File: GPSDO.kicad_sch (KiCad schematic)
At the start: 87 parts, among them J1 Conn_Coaxial, J10 PROG, J2 GPS_CONN, J3 Conn_Coaxial, J4 Conn_Coaxial, J5 Conn_Coaxial, J6 Conn_Coaxial, J7 LCD_CONN, J8 Barrel_Jack, J9 TOUCH_CONN, SW1 RESET_BTN, U1 REF3450, U10 MC7805BDTRKG, U11 74AUC1G74, U12 74AUC2G04, U13 74AUC2G04, U14 MC3487DX, U2 74LVC1G125SE-7, U3 AD5680, U4 NB3N551MN, U5 LTC2050IS8, U6 AVR32DB28x-xSO, U7 74LVC1G125SE-7, U8 74HC390, U9 L7805CV, X1 OCXO-14

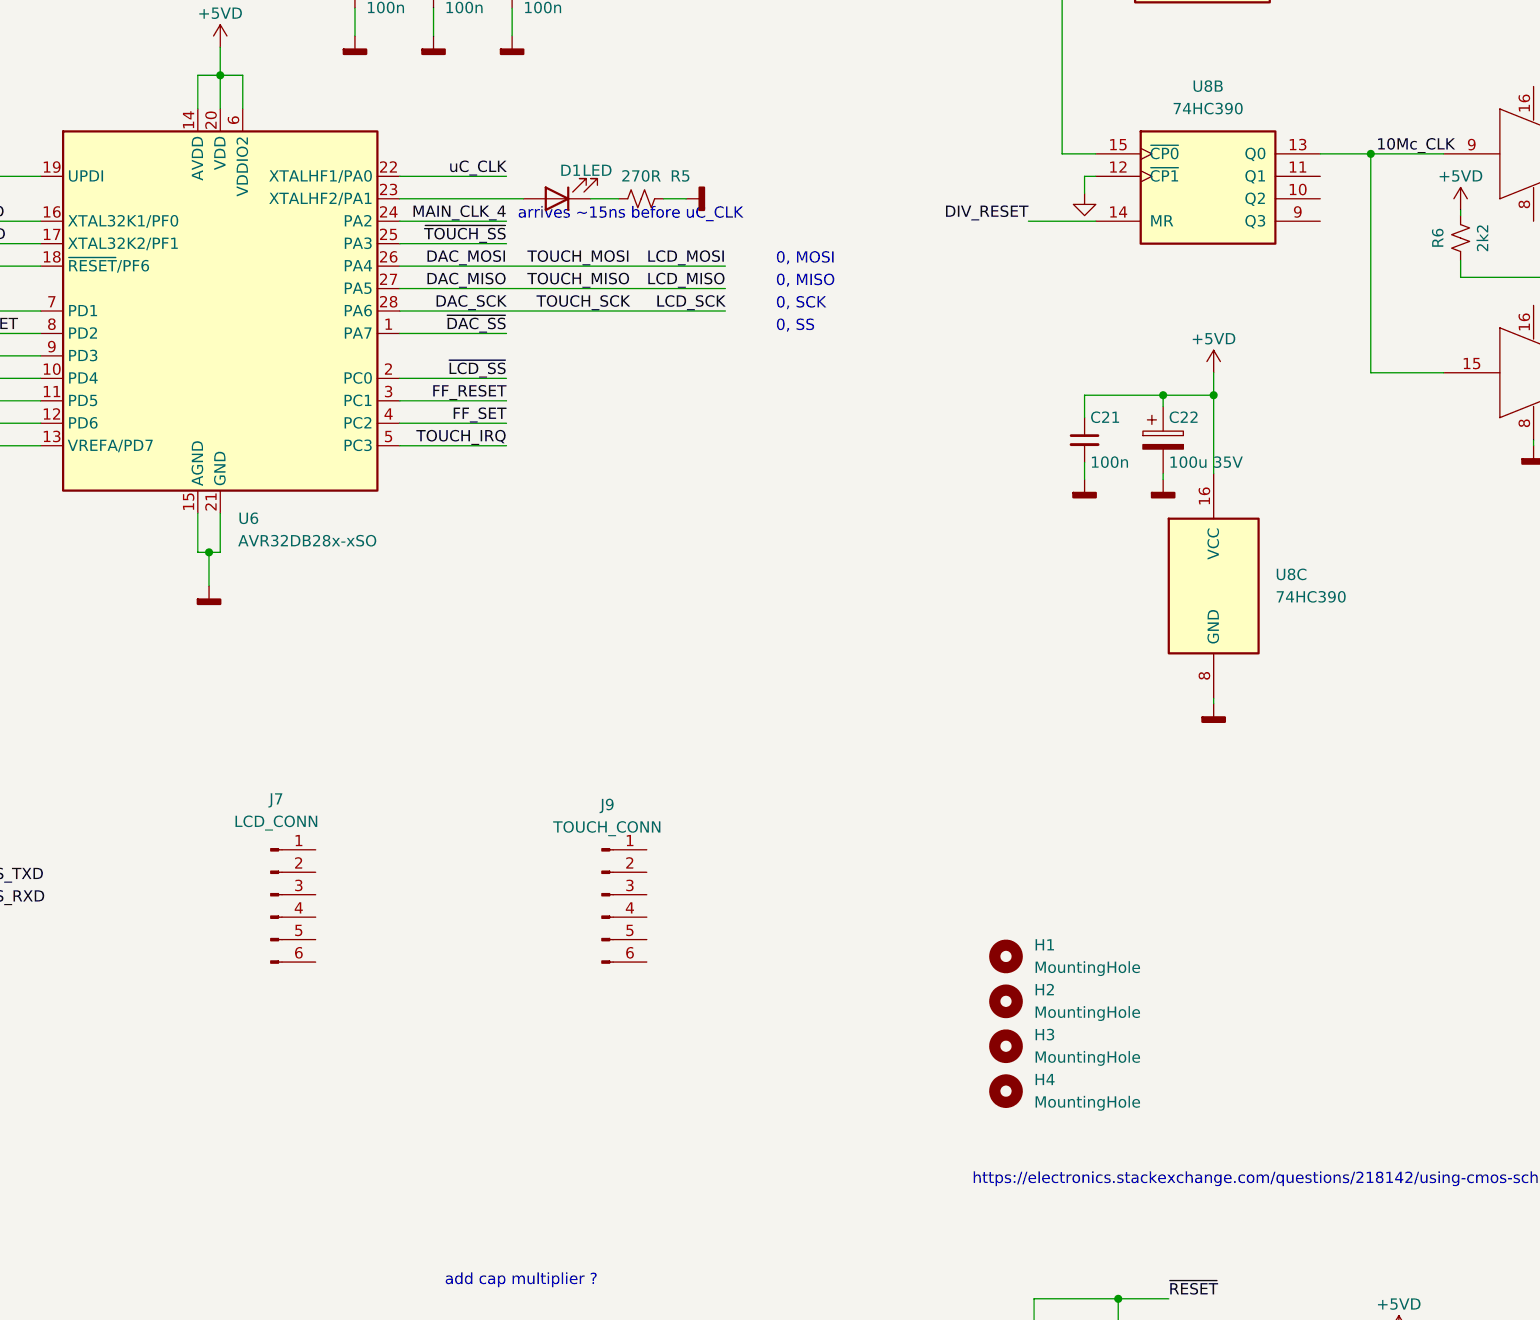
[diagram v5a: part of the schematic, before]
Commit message: LCD conn
Updated LCD & touch connector
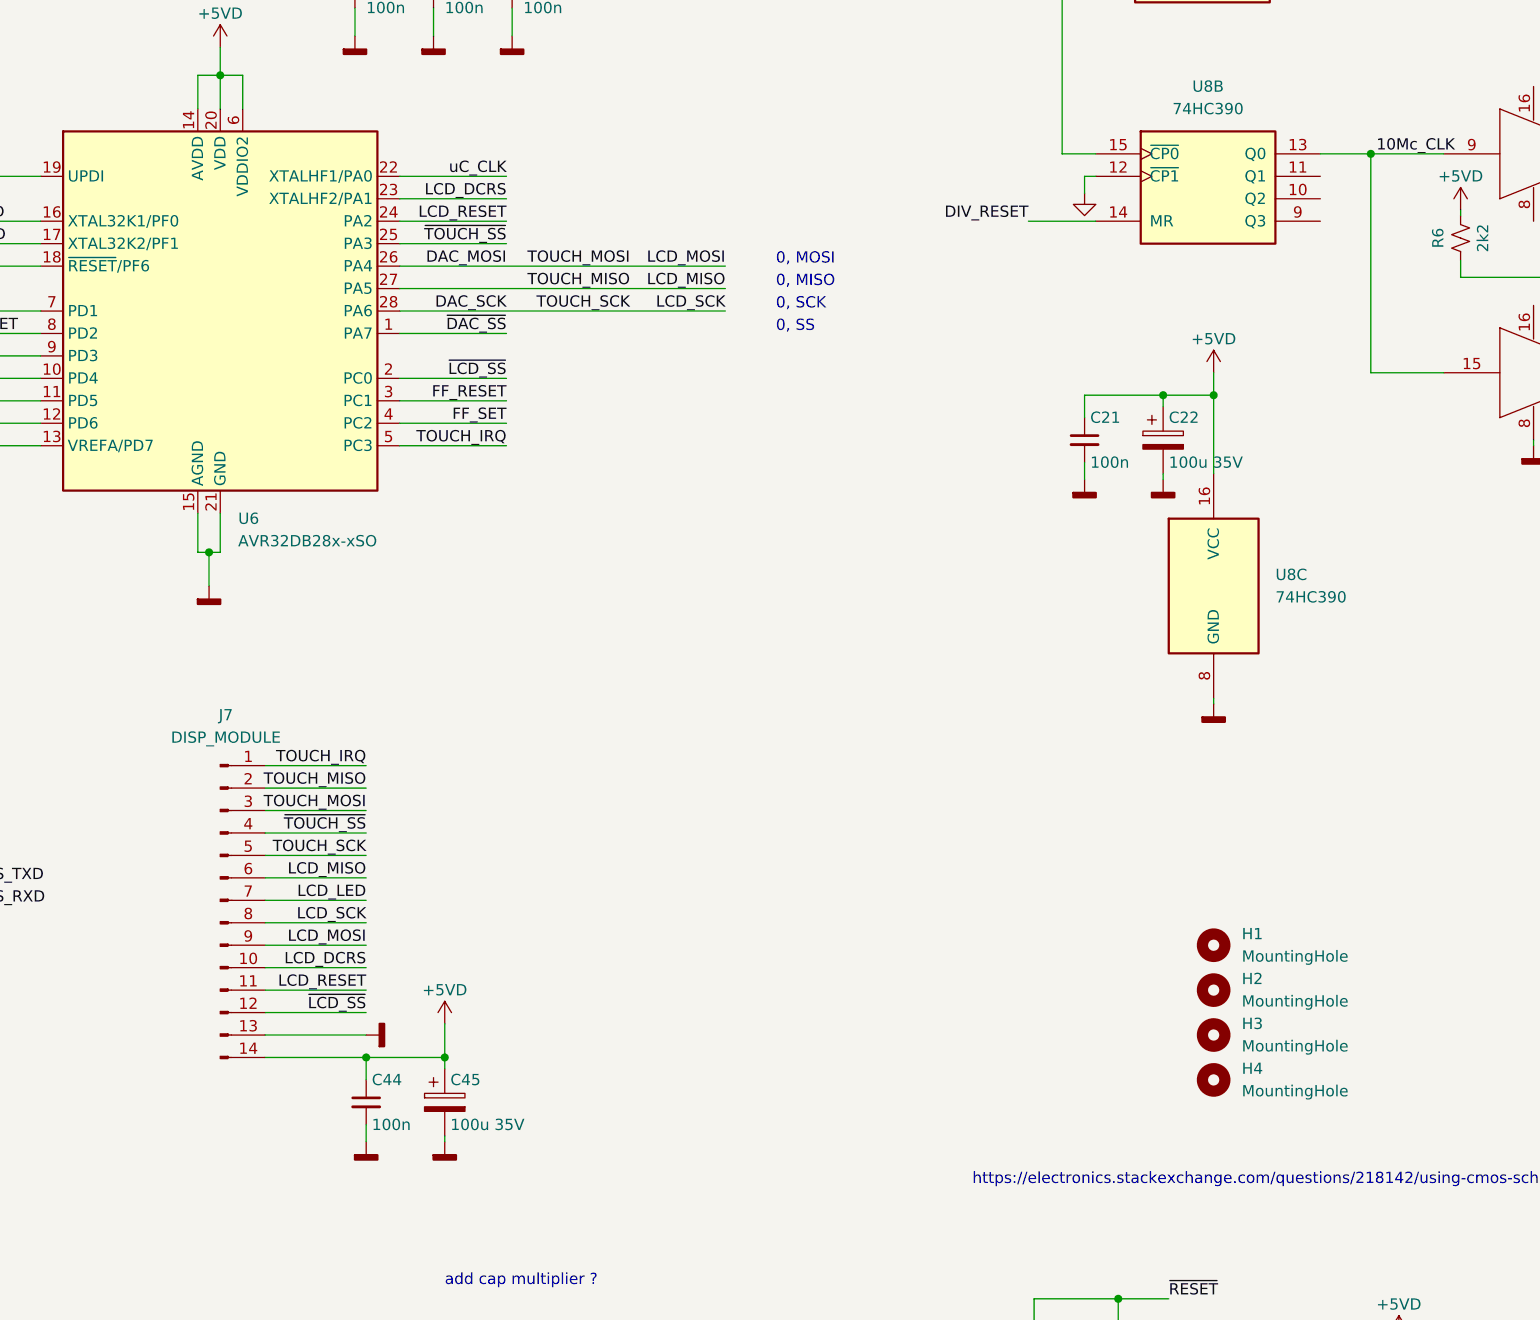
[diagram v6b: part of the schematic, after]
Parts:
- removed D1: LED, LED_SMD:LED_0805_2012Metric, symbol Device:LED
- removed J7: LCD_CONN, Connector_PinHeader_2.54mm:PinHeader_1x06_P2.54mm_Vertical, symbol Connector:Conn_01x06_Male
- removed J9: TOUCH_CONN, Connector_PinHeader_2.54mm:PinHeader_1x06_P2.54mm_Vertical, symbol Connector:Conn_01x06_Male
- removed R5: 270R, Resistor_SMD:R_0805_2012Metric_Pad1.20x1.40mm_HandSolder, symbol Device:R_Small_US
- added C44: 100n, Capacitor_SMD:C_0805_2012Metric_Pad1.18x1.45mm_HandSolder, symbol Device:C_Small
- added C45: 100u 35V, Capacitor_SMD:C_Elec_6.3x7.7, symbol Device:C_Polarized
- added J7: DISP_MODULE, Connector_PinHeader_2.54mm:PinHeader_1x14_P2.54mm_Vertical, symbol Connector:Conn_01x14_Male
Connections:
- net +5VD: now also C44.1, C45.1, J7.14 (Pin_14)
- net DAC_MOSI: now also J7.3 (Pin_3), J7.9 (Pin_9)
- net DAC_SCK: now also J7.5 (Pin_5), J7.8 (Pin_8)
- net GND: now also C44.2, C45.2, J7.13 (Pin_13)
- net MAIN_CLK_4: no longer U6.24 (PA2)
- net TOUCH_IRQ: now also J7.1 (Pin_1)
- net ~{LCD_SS}: now also J7.12 (Pin_12)
- net ~{TOUCH_SS}: now also J7.4 (Pin_4)
- net LCD_DCRS: now reaches U6.23 (XTALHF2/PA1)
- net LCD_DCRS: now also J7.10 (Pin_10)
- net DAC_MISO renamed LCD_MISO
- net LCD_MISO: now also J7.2 (Pin_2), J7.6 (Pin_6)
- new net LCD_LED: J7.7 (Pin_7)
- new net LCD_RESET: J7.11 (Pin_11), U6.24 (PA2)
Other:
- note removed: "arrives ~15ns before uC_CLK"
- moved on the sheet: H1, H2, H3, H4

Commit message: Updated output stage and a few bugs
Different driver, some layout moving
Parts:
- C29, C30, C36, C37, C38, C39, C40, C41: value 100n 10V MLCC -> 22nF 630V
- U14: value MC3487DX -> DS34C87T
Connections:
- net DAC_SLK is gone; now on net DAC_SCK: U3.6 (SCLK)
- net MAIN_CLK_1: no longer U8.15 (~{CP0}), U8.4 (~{CP1})
- net MAIN_CLK_3: now also U8.15 (~{CP0}), U8.4 (~{CP1}); no longer U12.1
- net MAIN_CLK_4: now also U12.1
- net 20Mc_CLK renamed MAIN_CLK_2
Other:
- note added: "20Mc CLK"
- note added: "Analog 100u 35V VZL101M1VTR-0810 8 Diam 10 L 0.16 Ohm 600 mA Digital 100u 35V VZL101M1VTR-0607 6.3 Diam 7.7 L 0.32 Ohm 290 mA DAC 10u 25V KAM32LL81E106KU 1210 output coupling: 1210CC223KAT2A"
- note added: "Decoupling caps for 10Mc Assume impedance below 2 Ohm for a 50 Ohm line, gives us a minimum of 8nF"
- note added: "TODO: - where to put trigger pin? - where to put ADC pin? -clock gen pow supply - check everything ok opn 5V? - (touch) display - serial interface - Main_clk_1 unused"
- note removed: "Analog 100u 35V VZL101M1VTR-0810 8 Diam 10 L 0.16 Ohm 600 mA Digital 100u 35V VZL101M1VTR-0607 6.3 Diam 7.7 L 0.32 Ohm 290 mA DAC 10u 25V KAM32LL81E106KU 1210"
- note removed: "TODO: - where to put trigger pin? - where to put ADC pin? -clock gen pow supply - check everything ok opn 5V? - (touch) display - serial interface -"
- note removed: "TODO: Decoupling caps for 10Mc with series resonance well above 100Mc"

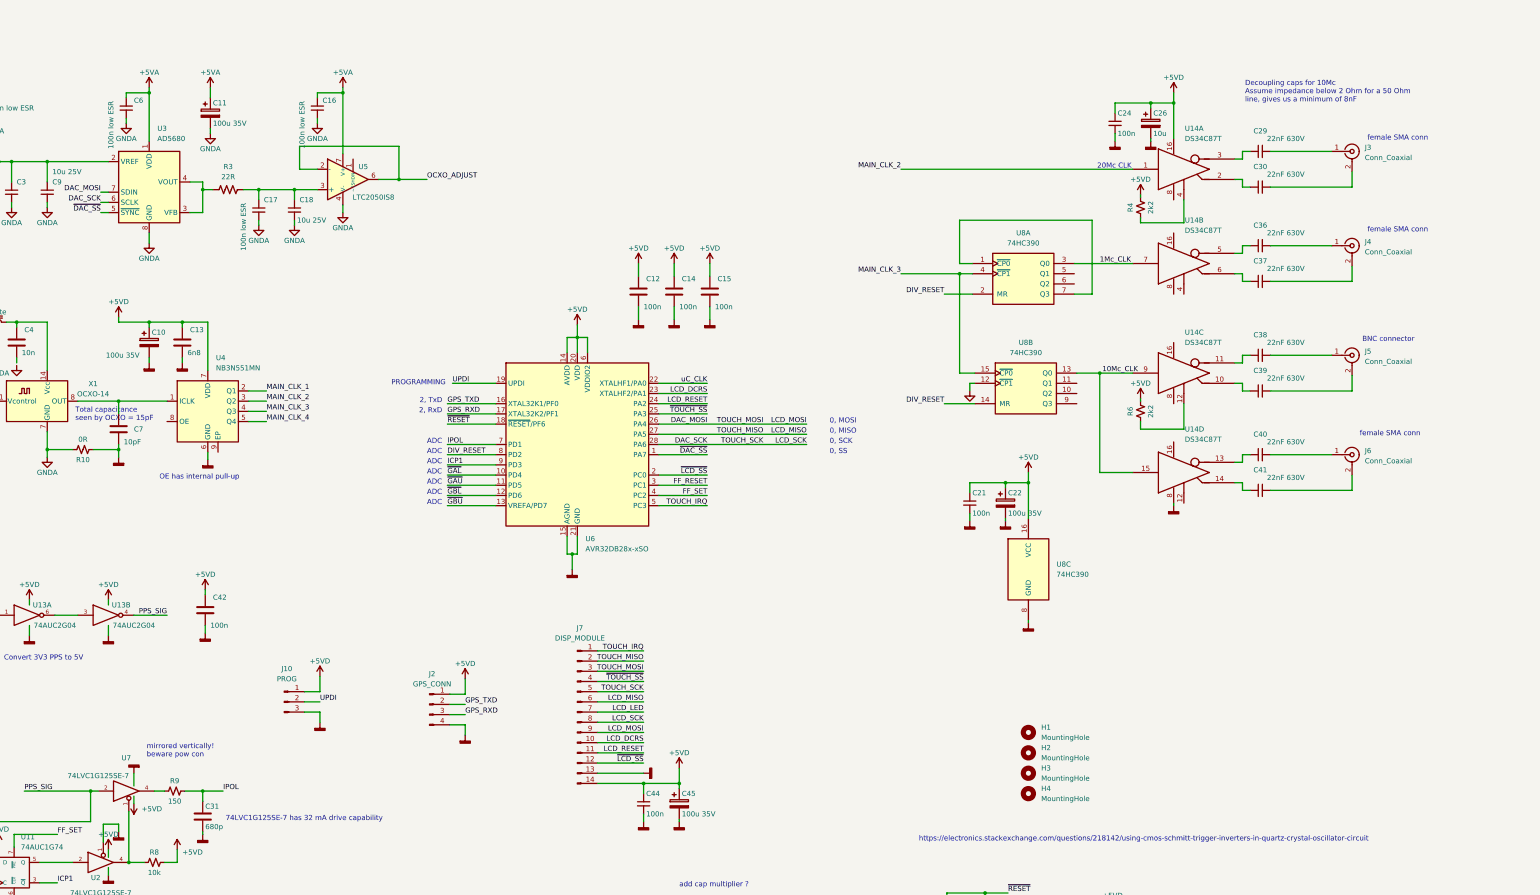
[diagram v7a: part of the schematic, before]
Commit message: finalised schematic
no more big changes
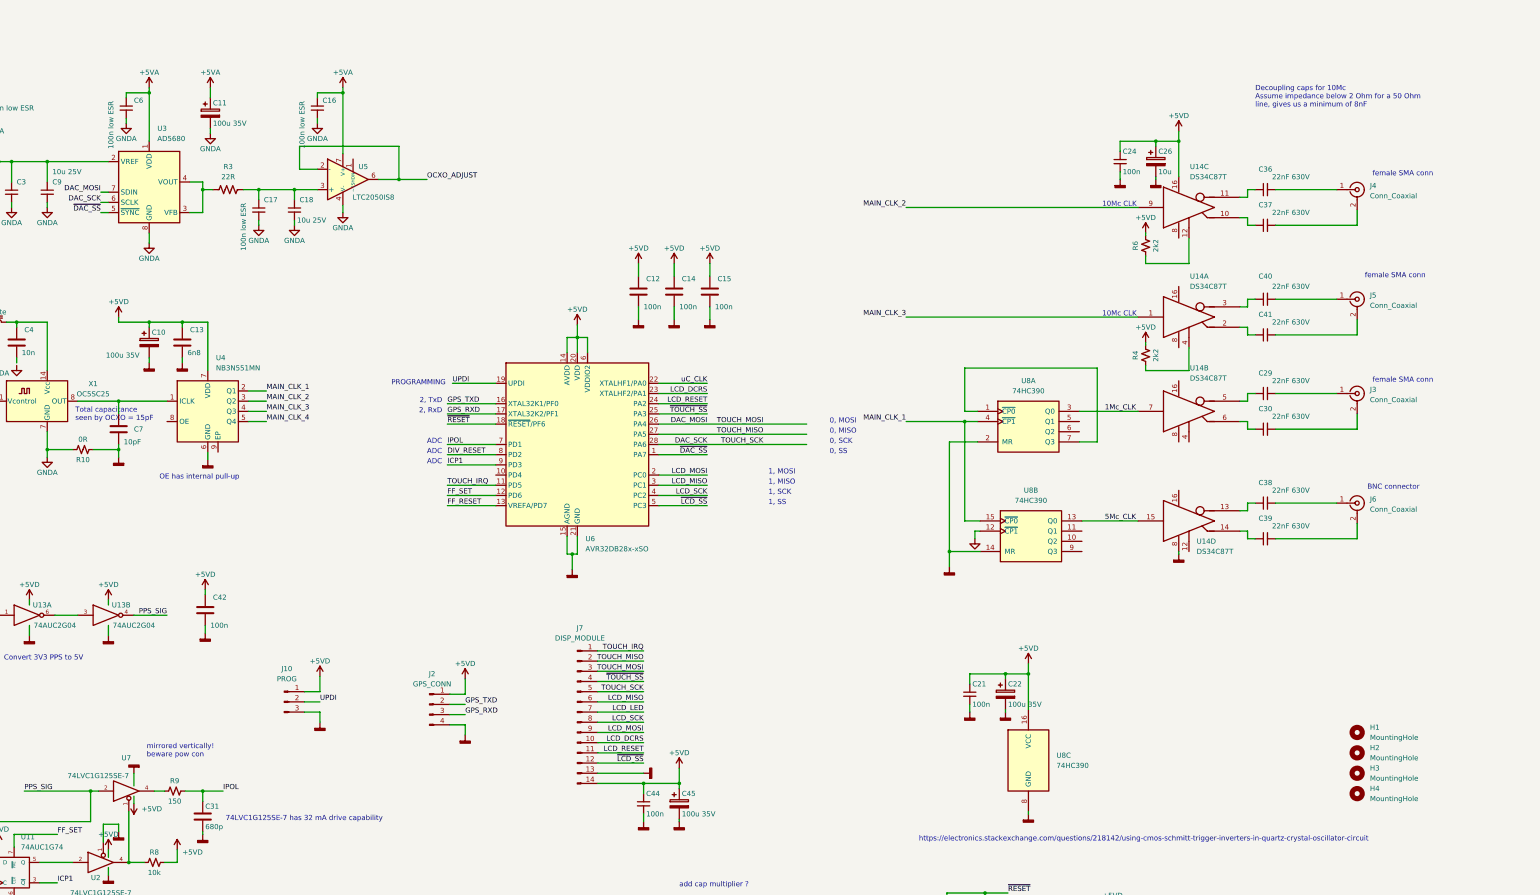
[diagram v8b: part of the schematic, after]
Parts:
- X1: value OCXO-14 -> OC5SC25
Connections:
- net ~{GAU} is gone; now on net TOUCH_IRQ: U6.11 (PD5)
- net ~{GBL} is gone; now on net FF_SET: U6.12 (PD6)
- net ~{GBU} is gone; now on net FF_RESET: U6.13 (VREFA/PD7)
- net +5VD: now also U14.16 (VCC); no longer U14.16 (VCC)
- net DAC_MOSI: no longer J7.9 (Pin_9)
- net DAC_SCK: no longer J7.8 (Pin_8)
- net DIV_RESET: no longer U8.14 (MR), U8.2 (MR)
- net FF_RESET: no longer U6.3 (PC1)
- net FF_SET: no longer U6.4 (PC2)
- net GND: now also U8.14 (MR), U8.2 (MR)
- net LCD_MISO: now also U6.3 (PC1); no longer J7.2 (Pin_2), U6.27 (PA5)
- net MAIN_CLK_1: now also U8.15 (~{CP0}), U8.4 (~{CP1})
- net MAIN_CLK_2: now also U14.9 (INPUT); no longer U14.1 (INPUT)
- net MAIN_CLK_3: now also U14.1 (INPUT); no longer U8.15 (~{CP0}), U8.4 (~{CP1})
- net TOUCH_IRQ: no longer U6.5 (PC3)
- net ~{LCD_SS}: now also U6.5 (PC3); no longer U6.2 (PC0)
- net at C29.1: now also U14.5 (OUT-); no longer U14.3 (OUT-)
- net at U14.13 (OUT-): now also C38.1; no longer C40.1
- net at U14.14 (OUT+): now also C39.1; no longer C41.1
- net at C36.1: now also U14.11 (OUT-); no longer U14.5 (OUT-)
- net at U14.6 (OUT+): now also C30.1; no longer C37.1
- net at U14.2 (OUT+): now also C41.1; no longer C30.1
- net at U14.10 (OUT+): now also C37.1; no longer C39.1
- net at C38.2: now also J6.1 (In); no longer J5.1 (In)
- net at C40.2: now also J5.1 (In); no longer J6.1 (In)
- net at J6.2 (Ext): now also C39.2; no longer C41.2
- net at J5.2 (Ext): now also C41.2; no longer C39.2
- net 10Mc_CLK renamed 5Mc_CLK
- net 5Mc_CLK: no longer U14.9 (INPUT)
- net ~{GAL}: no longer names the net of U6.10 (PD4)
- new net: C40.1, U14.3 (OUT-)
- new net LCD_MOSI: J7.9 (Pin_9), U6.2 (PC0)
- new net LCD_SCK: J7.8 (Pin_8), U6.4 (PC2)
- new net TOUCH_MISO: J7.2 (Pin_2), U6.27 (PA5)
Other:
- note added: "1, MISO"
- note added: "1, MOSI"
- note added: "1, SCK"
- note added: "1, SS"
- note added: "10Mc CLK"
- note removed: "20Mc CLK"
- moved on the sheet: C21, C22, C24, C26, C29, C30, C36, C37, C38, C39, C40, C41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
